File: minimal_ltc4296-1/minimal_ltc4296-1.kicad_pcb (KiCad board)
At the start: 4 copper layers, 38.1 x 30.5 mm, 28 parts, among them Q1 100.0 V, Q2 100.0 V, Q3 100.0 V, U1 LTC4296AUK-1-PBF

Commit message: Update KiCad PCB and schematic files
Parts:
- added Q4: 100.0 V, transistor_footprints:LFPAK33-8, F.Cu at (146.5, 89.1)
- added Q5: 100.0 V, transistor_footprints:LFPAK33-8, F.Cu at (137.9, 89.1)
- added Q6: 100.0 V, transistor_footprints:LFPAK33-8, F.Cu at (142.2, 89.1)
- added R17: 24 mΩ, resistor_footprints:R_0612_1632Metric, F.Cu at (146.5, 92.9)
- added R18: 24 mΩ, resistor_footprints:R_0612_1632Metric, F.Cu at (137.9, 92.9)
- added R19: 390 mΩ, resistor_footprints:R_0612_1632Metric, F.Cu at (142.2, 92.9)
- moved Q3 3.18 mm to (150.8, 89.1), turned to -90 degrees
- moved C2 3.16 mm to (141.7, 102.1), turned to -90 degrees
- moved R16 3.03 mm to (150.8, 92.9)
- moved Q2 2.91 mm to (155.1, 89.1), turned to -90 degrees
- moved R15 2.70 mm to (155.1, 92.9)
- moved C3 1.46 mm to (139.2, 102.0)
- moved D1 1.46 mm to (135.3, 103.0)
- moved R10 1.27 mm to (160.1, 100.7)
- moved R11 1.27 mm to (160.1, 96.4)
- moved R12 1.27 mm to (160.1, 109.3)
- moved R13 1.27 mm to (160.1, 105.0)
- moved R14 1.27 mm to (160.1, 113.6)
- moved C1 0.15 mm to (143.4, 102.0)
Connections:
- U1 pad 1: unconnected-(U1-OUTP0-Pad1) -> /OUTP0
- U1 pad 2: unconnected-(U1-HGATE0-Pad2) -> /HGATE0
- U1 pad 3: unconnected-(U1-HSNSM0-Pad3) -> /HSNSM0
- U1 pad 4: unconnected-(U1-HSNSP0-Pad4) -> /PSE
- U1 pad 41: unconnected-(U1-OUTP2-Pad41) -> /OUTP2
- U1 pad 42: unconnected-(U1-HGATE2-Pad42) -> /HGATE2
- U1 pad 43: unconnected-(U1-HSNSM2-Pad43) -> /HSNSM2
- U1 pad 44: unconnected-(U1-HSNSP2-Pad44) -> /PSE
- U1 pad 45: unconnected-(U1-OUTP1-Pad45) -> /OUTP1
- U1 pad 46: unconnected-(U1-HGATE1-Pad46) -> /HGATE1
- U1 pad 47: unconnected-(U1-HSNSM1-Pad47) -> /HSNSM1
- U1 pad 48: unconnected-(U1-HSNSP1-Pad48) -> /PSE
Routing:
- net /PSE: track 3.73 -> 14.7 mm, vias 9 -> 12
- net /OUTP3: track 0.00 -> 3.01 mm, vias 0 -> 1
- net /OUTP0: track 0.00 -> 3.01 mm, vias 0 -> 1
- net /HSNSM1: track 0.00 -> 2.90 mm, vias 0 -> 1
- net /HGATE3: track 0.00 -> 2.90 mm, vias 0 -> 1
- net /HGATE0: track 0.00 -> 2.90 mm, vias 0 -> 1
- net /HGATE1: track 0.00 -> 2.79 mm, vias 0 -> 1
- net /HSNSM3: track 0.00 -> 2.79 mm, vias 0 -> 1
- net /HSNSM0: track 0.00 -> 2.79 mm, vias 0 -> 1
- net /OUTP1: track 0.00 -> 2.69 mm, vias 0 -> 1
- net /OUTP2: track 0.00 -> 2.58 mm, vias 0 -> 1
- net /HSNSM2: track 0.00 -> 2.47 mm, vias 0 -> 1
- net /HGATE2: track 0.00 -> 2.47 mm, vias 0 -> 1
- net /LSNS: track 23.8 -> 26.2 mm
- net /OUTM2: track 8.93 -> 10.2 mm
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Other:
- board size 38.1 x 30.5 mm -> 38.1 x 31.8 mm

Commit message: Update PCB file
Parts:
- moved Q5 4.08 mm to (141.2, 86.8)
- moved Q6 3.72 mm to (145.1, 86.8)
- moved R18 3.58 mm to (141.2, 91.8), turned to 0 degrees
- moved Q4 3.37 mm to (148.9, 86.8)
- moved R19 3.16 mm to (145.1, 91.8), turned to 0 degrees
- moved Q3 3.05 mm to (152.8, 86.8)
- moved Q2 2.77 mm to (156.7, 86.8)
- moved R17 2.74 mm to (148.9, 91.8), turned to 0 degrees
- moved R16 2.34 mm to (152.8, 91.8), turned to 0 degrees
- moved R15 1.96 mm to (156.7, 91.8), turned to 0 degrees
- moved R10 1.27 mm to (161.3, 100.7)
- moved R11 1.27 mm to (161.3, 96.4)
- moved R12 1.27 mm to (161.3, 109.3)
- moved R13 1.27 mm to (161.3, 105.0)
- moved R14 1.27 mm to (161.3, 113.6)
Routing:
- net /PSE: track 14.7 -> 34.7 mm, vias 12 -> 17
- net /OUTP4: track 2.89 -> 20.8 mm, vias 1 -> 2
- net /HGATE4: track 3.00 -> 20.7 mm, vias 1 -> 2
- net /HGATE0: track 2.90 -> 19.7 mm, vias 1 -> 2
- net /OUTP0: track 3.01 -> 17.8 mm, vias 1 -> 2
- net /HGATE1: track 2.79 -> 17.1 mm, vias 1 -> 2
- net /HGATE3: track 2.90 -> 17.1 mm, vias 1 -> 2
- net /HGATE2: track 2.47 -> 16.4 mm, vias 1 -> 2
- net /OUTP3: track 3.01 -> 16.4 mm, vias 1 -> 2
- net /OUTP1: track 2.69 -> 16.0 mm, vias 1 -> 2
- net /OUTP2: track 2.58 -> 15.6 mm, vias 1 -> 2
- net /HSNSM0: track 2.79 -> 9.24 mm, vias 1 -> 2
- net /HSNSM4: track 3.11 -> 8.40 mm, vias 1 -> 2
- net /LSNS: track 26.2 -> 30.0 mm
- net /HSNSM3: track 2.79 -> 5.68 mm, vias 1 -> 2
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- added copper zone on F.Cu, net /HSNSM0
- added copper zone on F.Cu, net /HSNSM1
- added copper zone on F.Cu, net /HSNSM2
- added copper zone on F.Cu, net /HSNSM3
- added copper zone on F.Cu, net /HSNSM4
- added copper zone on F.Cu, net /OUTP0
- added copper zone on F.Cu, net /OUTP1
- added copper zone on F.Cu, net /OUTP2
- added copper zone on F.Cu, net /OUTP3
- added copper zone on F.Cu, net /OUTP4
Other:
- board size 38.1 x 31.8 mm -> 38.1 x 35.6 mm

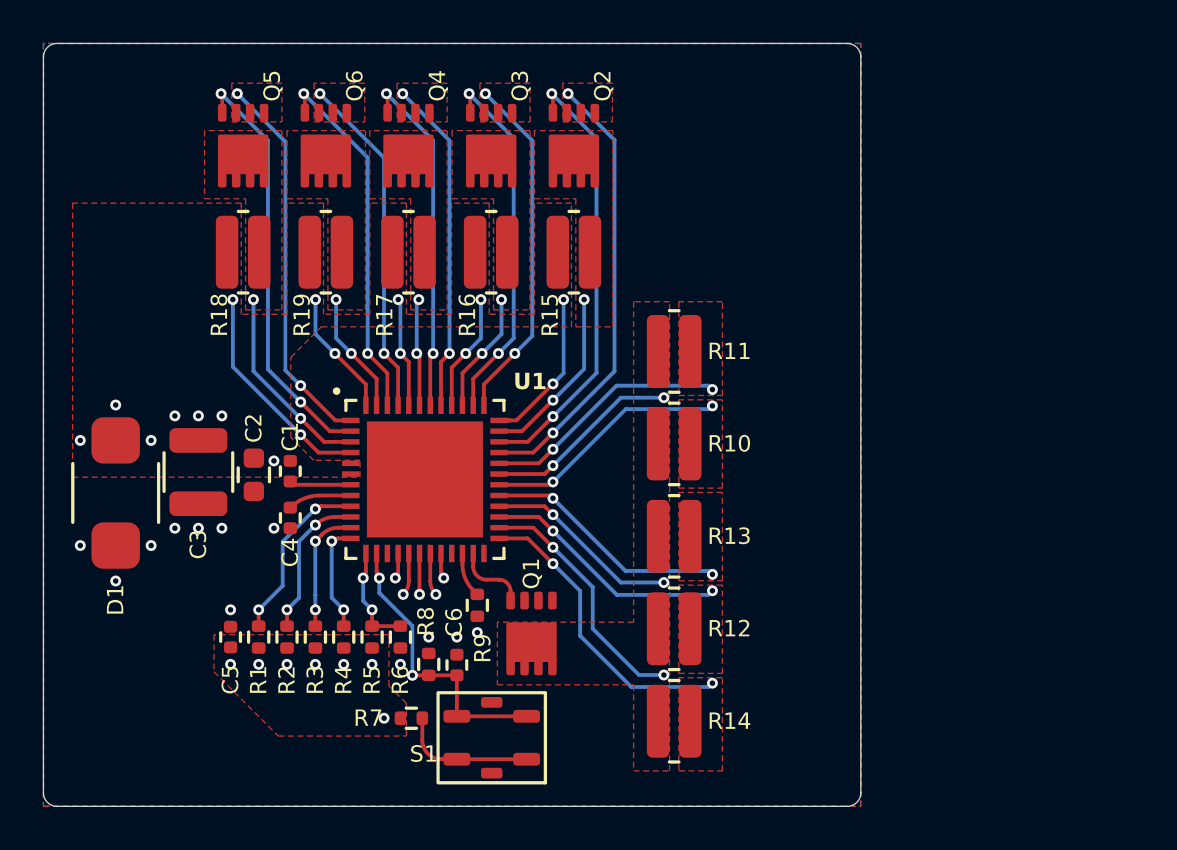
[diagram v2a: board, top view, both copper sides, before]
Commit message: Update KiCAD files and generator
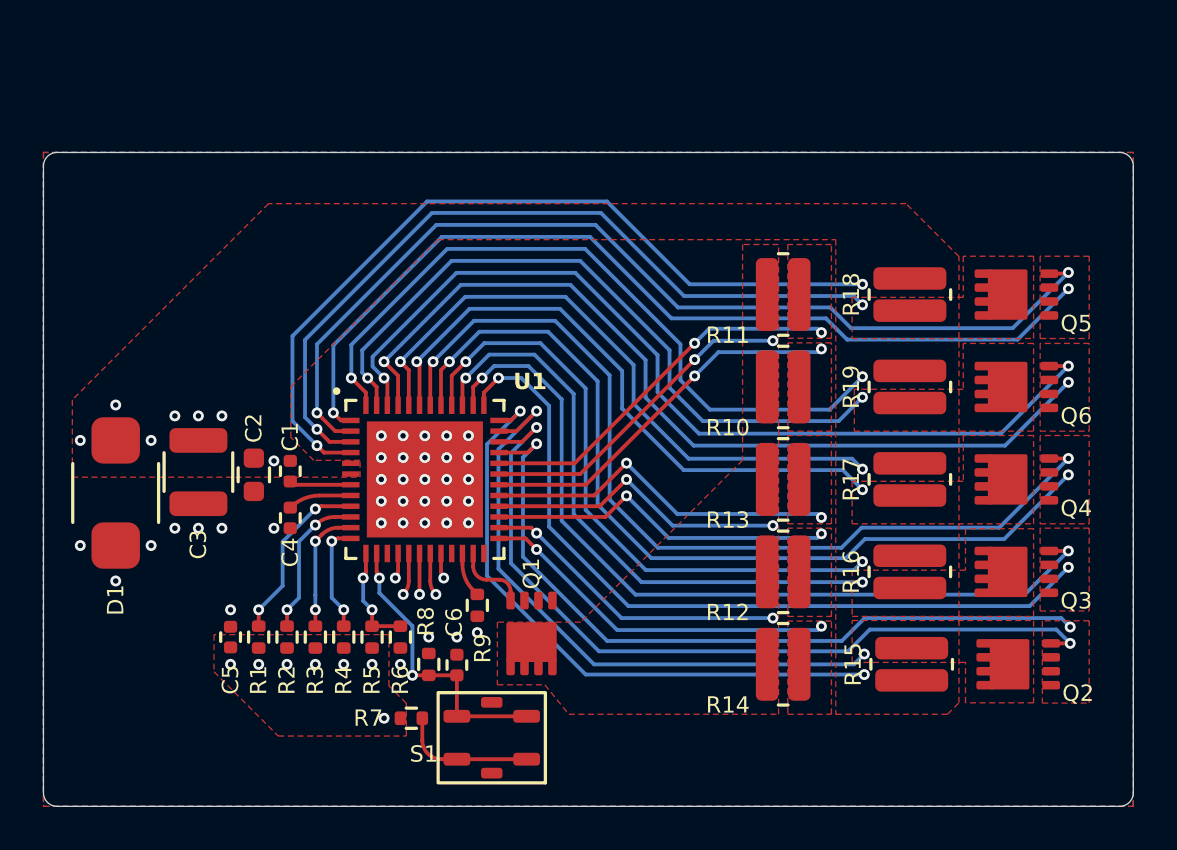
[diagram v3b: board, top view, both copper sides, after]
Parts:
- moved Q5 36.7 mm to (177.3, 93.7), turned to 180 degrees
- moved Q6 34.1 mm to (177.3, 98.1), turned to 180 degrees
- moved Q4 32.3 mm to (177.3, 102.4), turned to 180 degrees
- moved Q2 31.8 mm to (177.4, 111.0), turned to 180 degrees
- moved Q3 31.5 mm to (177.3, 106.7), turned to 180 degrees
- moved R18 31.1 mm to (172.3, 93.7), turned to -90 degrees
- moved R19 27.9 mm to (172.3, 98.1), turned to -90 degrees
- moved R17 25.7 mm to (172.3, 102.4), turned to -90 degrees
- moved R15 24.8 mm to (172.4, 111.0), turned to 90 degrees
- moved R16 24.6 mm to (172.3, 106.7), turned to -90 degrees
- moved R10 5.73 mm to (166.4, 98.1)
- moved R11 5.73 mm to (166.4, 93.7)
- moved R13 5.73 mm to (166.4, 102.4)
- moved R12 5.73 mm to (166.4, 106.7)
- moved R14 5.73 mm to (166.4, 111.0)
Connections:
- net Net-(Q1-G) renamed /LGATE
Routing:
- net /PSE: track 34.7 -> 159.4 mm
- net /HSNSM0: track 9.24 -> 36.4 mm
- net /HSNSM1: track 5.71 -> 32.5 mm
- net /HGATE0: track 19.7 -> 46.4 mm
- net /HGATE2: track 16.4 -> 42.9 mm
- net /HGATE1: track 17.1 -> 42.9 mm
- net /OUTP0: track 17.8 -> 43.4 mm
- net /OUTP2: track 15.6 -> 41.0 mm
- net /OUTP1: track 16.0 -> 41.0 mm
- net /HSNSM2: track 5.02 -> 28.4 mm
- net /HSNSM3: track 5.68 -> 28.0 mm
- net /HGATE3: track 17.1 -> 38.5 mm
- net /HSNSM4: track 8.40 -> 29.3 mm
- net /OUTP3: track 16.4 -> 36.6 mm
- net /HGATE4: track 20.7 -> 38.2 mm
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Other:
- board size 38.1 x 35.6 mm -> 50.8 x 30.5 mm

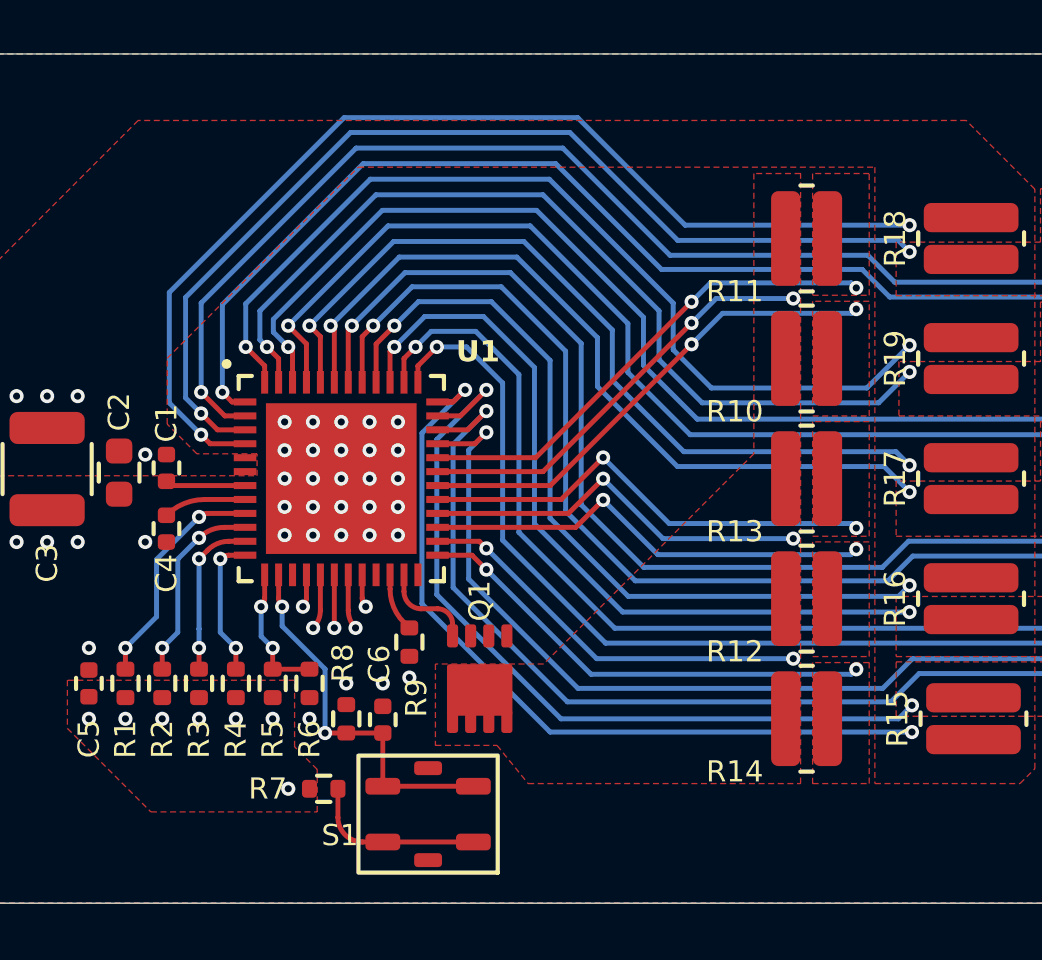
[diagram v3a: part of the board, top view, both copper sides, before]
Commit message: Update PCB layout and schematic, refresh symbol library
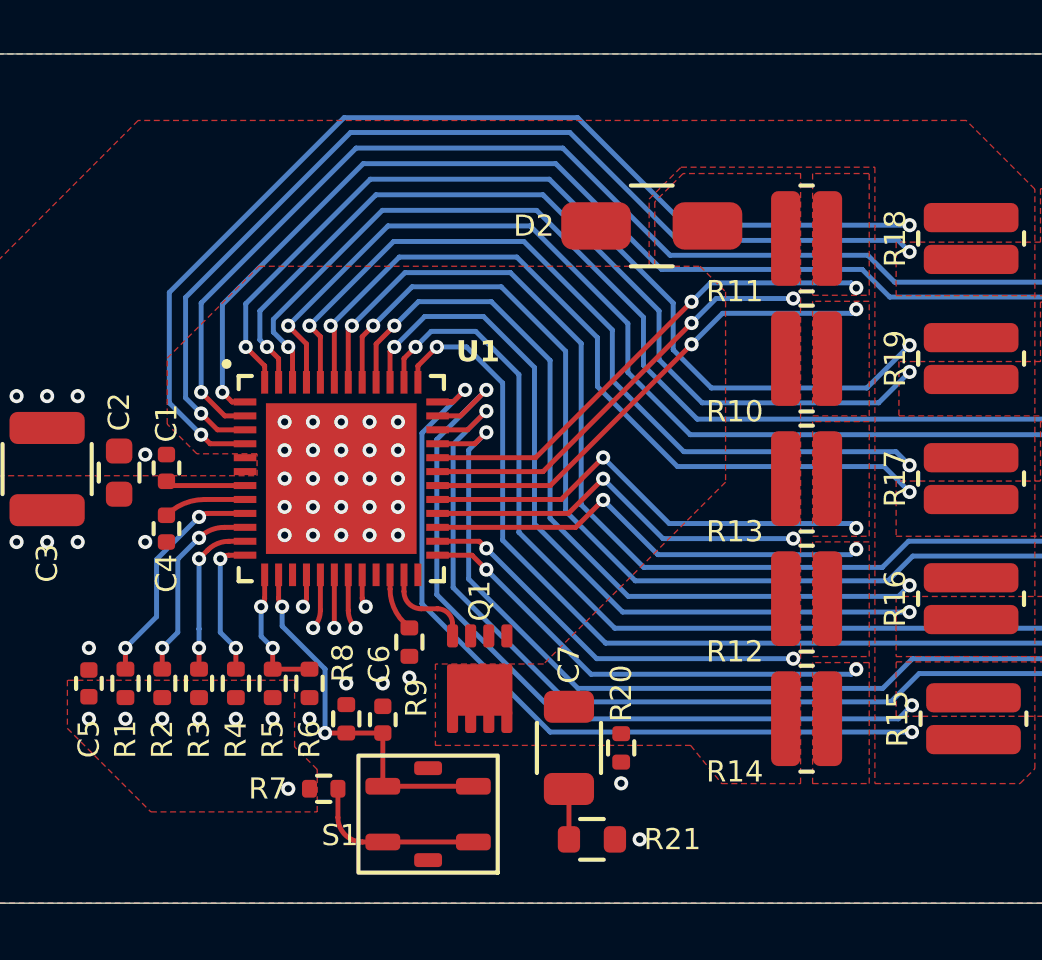
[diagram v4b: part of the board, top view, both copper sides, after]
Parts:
- added C7: 2.2 µF, capacitor_footprints:C_1206_3216Metric, F.Cu at (157.9, 112.0)
- added D2: 100 V, diode_footprints:SMA, F.Cu at (160.9, 93.3)
- added R20: 49.9 kΩ, resistor_footprints:R_0402_1005Metric, F.Cu at (159.8, 112.0)
- added R21: 0 mΩ, resistor_footprints:R_0603_1608Metric, F.Cu at (158.7, 115.3)
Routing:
- net Net-(C7-Pad1): track 0.00 -> 1.81 mm
- net GND: vias 37 -> 39

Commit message: Update PCB layout and schematic
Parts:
- added J1: TBP02R1-381-03BE, connector_footprints:TBP02R1-381-03BE, F.Cu at (183.2, 75.1)
- added J2: TBP02R1-381-03BE, connector_footprints:TBP02R1-381-03BE, F.Cu at (183.2, 129.6)
- added J3: TBP02R1-381-03BE, connector_footprints:TBP02R1-381-03BE, F.Cu at (183.2, 102.4)
- added J4: TBP02R1-381-03BE, connector_footprints:TBP02R1-381-03BE, F.Cu at (183.2, 88.7)
- added J5: TBP02R1-381-03BE, connector_footprints:TBP02R1-381-03BE, F.Cu at (183.2, 116.0)
- C7: footprint capacitor_footprints:C_1206_3216Metric -> capacitor_footprints:C_0805_2012Metric
- R20: footprint resistor_footprints:R_0402_1005Metric -> resistor_footprints:R_0805_2012Metric
- R21: footprint resistor_footprints:R_0603_1608Metric -> resistor_footprints:R_0805_2012Metric
- moved Q5 38.2 mm to (140.3, 84.3), turned to -90 degrees
- moved Q6 35.4 mm to (144.6, 84.3), turned to -90 degrees
- moved Q4 33.6 mm to (148.9, 84.3), turned to -90 degrees
- moved Q2 33.3 mm to (157.6, 84.2), turned to -90 degrees
- moved Q3 32.8 mm to (153.2, 84.3), turned to -90 degrees
- moved R18 32.3 mm to (140.3, 89.2), turned to 0 degrees
- moved R19 29.1 mm to (144.6, 89.2), turned to 0 degrees
- moved R17 26.8 mm to (148.9, 89.2), turned to 0 degrees
- moved R15 26.4 mm to (157.6, 89.1), turned to 180 degrees
- moved D2 26.0 mm to (159.5, 119.2)
- moved R16 25.8 mm to (153.2, 89.2), turned to 0 degrees
- moved R14 18.3 mm to (176.1, 95.4), turned to 90 degrees
- moved R12 12.5 mm to (171.8, 95.4), turned to 90 degrees
- moved R11 7.76 mm to (158.8, 95.4), turned to 90 degrees
- moved R13 7.01 mm to (167.4, 95.4), turned to 90 degrees
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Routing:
- net /PSE: track 159.4 -> 51.9 mm, vias 17 -> 18
- net /HSNSM0: track 36.4 -> 12.0 mm
- net /HSNSM1: track 32.5 -> 8.33 mm
- net /HGATE0: track 46.4 -> 22.6 mm
- net /HGATE2: track 42.9 -> 19.3 mm
- net /HGATE1: track 42.9 -> 19.7 mm
- net /OUTP0: track 43.4 -> 20.7 mm
- net /OUTP2: track 41.0 -> 18.4 mm
- net /OUTP1: track 41.0 -> 18.7 mm
- net /HSNSM2: track 28.4 -> 7.67 mm
- net /HSNSM3: track 28.0 -> 8.52 mm
- net /HGATE3: track 38.5 -> 20.0 mm
- net /HSNSM4: track 29.3 -> 11.3 mm
- net /OUTP3: track 36.6 -> 19.2 mm
- net /HGATE4: track 38.2 -> 23.8 mm
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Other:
- board size 50.8 x 30.5 mm -> 53.3 x 71.1 mm

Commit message: Update PCB layout
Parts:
- moved J2 61.1 mm to (177.0, 68.9), turned to 0 degrees
- moved J1 61.1 mm to (122.5, 68.9), turned to 0 degrees
- moved J5 51.1 mm to (163.3, 68.9), turned to 0 degrees
- moved J4 51.1 mm to (136.1, 68.9), turned to 0 degrees
- moved J3 47.4 mm to (149.7, 68.9), turned to 0 degrees
- moved D2 25.9 mm to (152.4, 94.4)
- moved R11 19.3 mm to (178.1, 95.4)
- moved R14 17.2 mm to (158.8, 95.4)
- moved R10 10.1 mm to (173.3, 95.4)
- moved R12 8.11 mm to (163.6, 95.4)
- moved R13 1.02 mm to (168.5, 95.4)
- moved R15 0.09 mm to (157.6, 89.2), turned to 0 degrees
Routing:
- net /OUTM4: track 11.9 -> 30.6 mm
- net /LSNS: track 54.6 -> 69.1 mm
- net /OUTM3: track 13.8 -> 26.9 mm
- net /OUTM0: track 27.8 -> 18.2 mm
- net /OUTM2: track 20.8 -> 25.6 mm
- net /OUTM1: track 23.0 -> 19.0 mm
- net /PSE: track 51.9 -> 51.3 mm
- removed copper zone on In1.Cu, net /LSNS
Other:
- board size 53.3 x 71.1 mm -> 71.1 x 50.8 mm

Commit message: Update PCB and schematic files, and KiCAD symbols generator
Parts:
- added J6: TBP02R1-381-02BE, connector_footprints:TBP02R1-381-02BE, F.Cu at (116.3, 102.0)
- moved R11 20.3 mm to (171.1, 114.4), turned to 0 degrees
- moved R10 14.4 mm to (171.1, 109.6), turned to 0 degrees
- moved R14 12.2 mm to (171.1, 95.2), turned to 0 degrees
- moved R13 9.73 mm to (171.1, 104.8), turned to 0 degrees
- moved R12 8.70 mm to (171.1, 100.0), turned to 0 degrees
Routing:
- net /OUTM0: track 18.2 -> 23.6 mm
- net /OUTM1: track 19.0 -> 23.7 mm
- net /OUTM3: track 26.9 -> 30.7 mm
- net /LSNS: track 69.1 -> 72.8 mm
- net /OUTM4: track 30.6 -> 33.2 mm

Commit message: Update PCB layout
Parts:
- moved R10 7.26 mm to (163.8, 109.3)
- moved R11 7.26 mm to (163.8, 114.1)
- moved R13 7.26 mm to (163.8, 104.5)
- moved R14 7.26 mm to (163.8, 94.9)
- moved R12 7.26 mm to (163.8, 99.7)
- moved D2 5.69 mm to (158.1, 94.9)
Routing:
- net /LSNS: track 72.8 -> 46.1 mm
- net /OUTM3: track 30.7 -> 16.3 mm
- net /OUTM2: track 25.6 -> 13.7 mm
- net /OUTM4: track 33.2 -> 21.4 mm
- net /OUTM1: track 23.7 -> 17.6 mm
- net /OUTM0: track 23.6 -> 17.8 mm
- net /PSE: track 51.3 -> 52.0 mm
